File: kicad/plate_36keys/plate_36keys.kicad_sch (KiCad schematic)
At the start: 54 parts, among them SW1 EC_SW, SW36 EC_SW

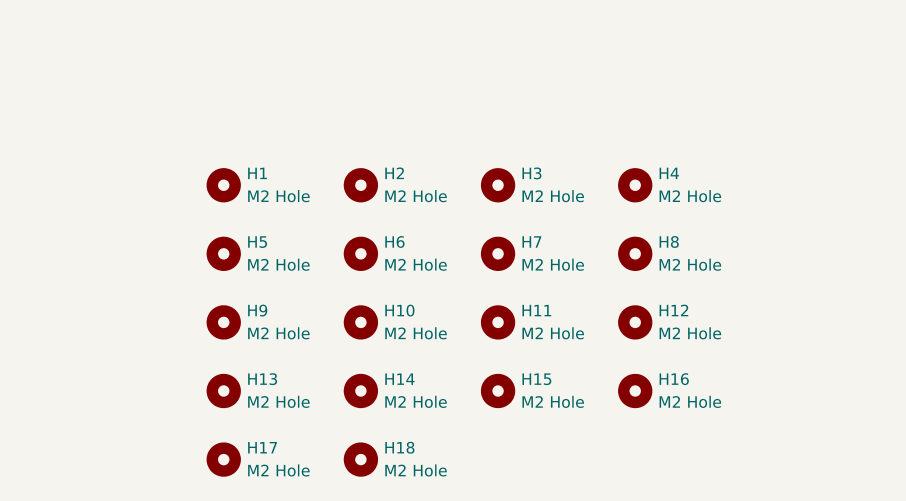
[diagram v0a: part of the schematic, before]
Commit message: Clean up after prototyping
- Doc update
- remove uncessary files
- remove two more mounting holes in the "chiffre gap" area
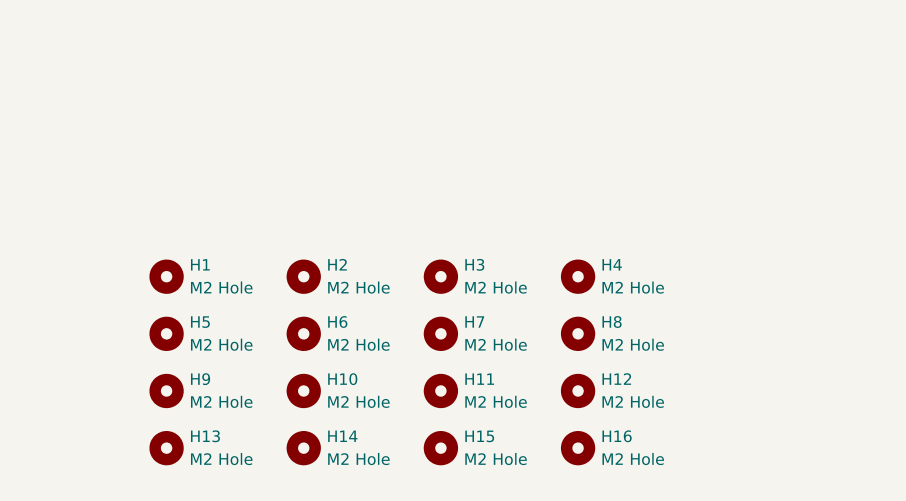
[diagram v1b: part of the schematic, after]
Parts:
- removed H17, H18: M2 Hole, capacitive_sensors:MountingHole_1.6mm_M2_tapped, symbol Mechanical:MountingHole

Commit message: Remove extra mounting holes from PCB and update version number.
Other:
- title: Le Capybara -> Le Capybara Plate (36 keys)
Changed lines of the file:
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@@
   (paper "A4")
   (title_block
-    (title "Le Capybara")
-    (date "2023-07-08")
-    (rev "0.2")
+    (title "Le Capybara Plate (36 keys)")
+    (date "2024-02-21")
+    (rev "1.0")
     (company "sporkus")
   )
